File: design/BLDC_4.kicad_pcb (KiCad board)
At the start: 4 copper layers, 38.5 x 65 mm, 126 parts, among them K1 SERVO, P1 HALL/Encoder, P101 CANBUS, P2 SWD, P3 PWR_COMM, P4 IN+, P5 IN-, P6 MOTOR1, P7 MOTOR2, P9 MOTOR3, Q1 IRFS7530, Q2 IRFS7530, Q3 IRFS7530, Q4 IRFS7530, Q5 IRFS7530, Q6 IRFS7530, U1 STM32F40X_LQFP64, U2 TC2117, U3 DRV8302, U401 SN65HVD232, X1 MINI-USB-SHIELD-32005-201, X2 8MHz 10ppm

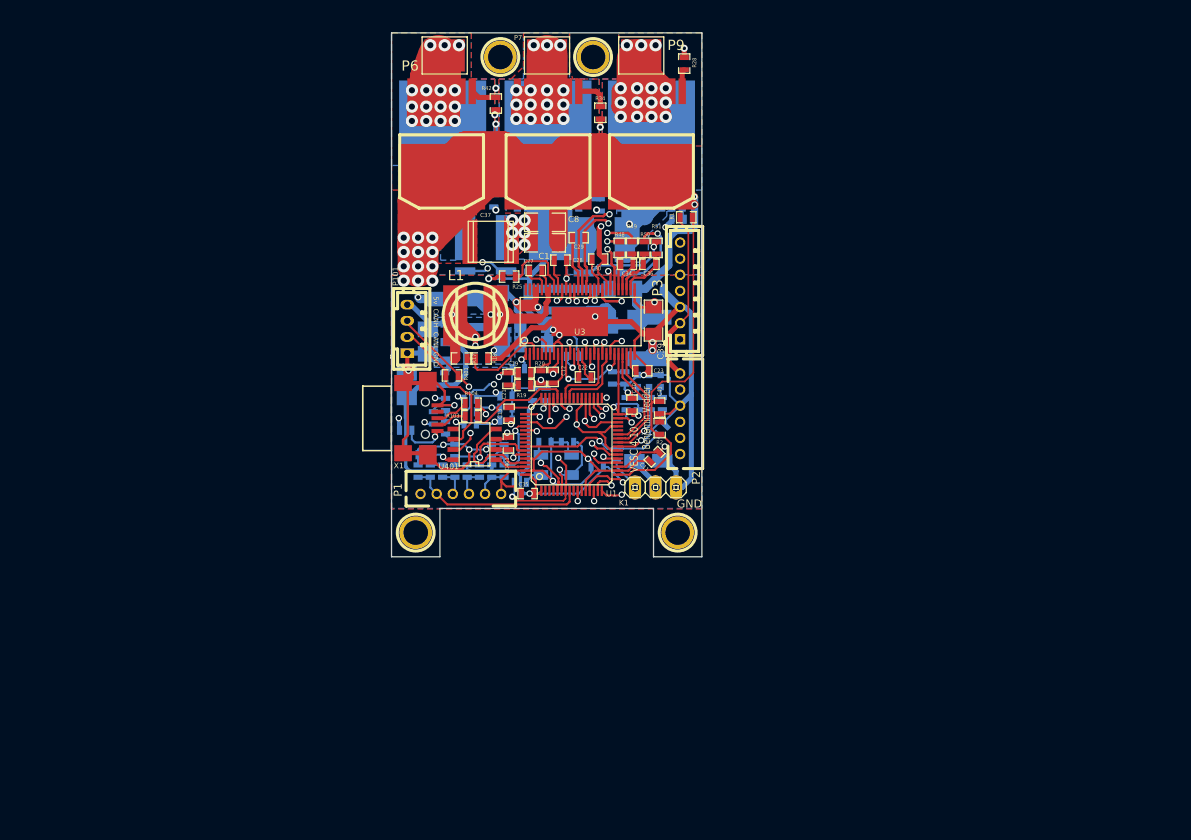
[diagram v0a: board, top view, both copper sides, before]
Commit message: schema mods done
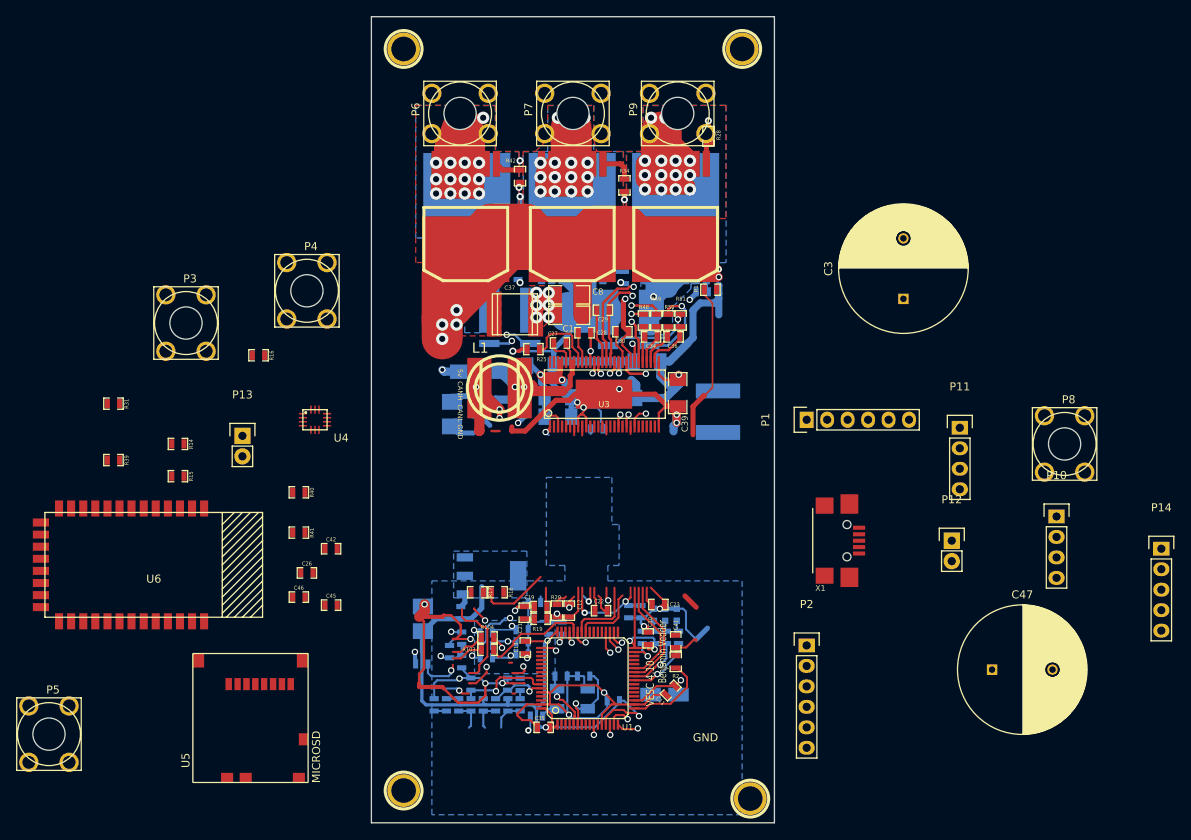
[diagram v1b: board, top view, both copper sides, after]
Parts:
- removed C401: 2.2u, CRF1:SMD-0603_c
- removed K1: SERVO, CRF1:pinhead-1X03
- removed P101: CANBUS, JST conn:b4b-ph-kl
- removed R401: NI, CRF1:SMD-0603_r
- removed R402: 10k, CRF1:SMD-0603_r
- removed R5: 2k2, CRF1:SMD-0603_r
- removed U401: SN65HVD232, CRF1:SOIC-8-W
- added C26: 2.2u, CRF1:SMD-0603_c, F.Cu at (68.0, 147.0)
- added C42: 100nF, CRF1:SMD-0603_c, F.Cu at (71.0, 144.0)
- added C45: 100nF, CRF1:SMD-0603_c, F.Cu at (71.0, 151.0)
- added C46: 2.2u, CRF1:SMD-0603_c, F.Cu at (67.0, 150.0)
- added C47: 680µF, Capacitors_ThroughHole:C_Radial_D16_L25_P7.5, F.Cu at (153.0, 159.0)
- added P10: EXT_I2C, Pin_Headers:Pin_Header_Straight_1x04, F.Cu at (161.0, 140.0)
- added P11: OLED, Pin_Headers:Pin_Header_Straight_1x04, F.Cu at (149.0, 129.0)
- added P12: BRAKE, Pin_Headers:Pin_Header_Straight_1x02, F.Cu at (148.0, 143.0)
- added P13: BUTTONS, Pin_Headers:Pin_Header_Straight_1x02, F.Cu at (60.0, 130.0)
- added P14: EXTENSION, Pin_Headers:Pin_Header_Straight_1x05, F.Cu at (174.0, 144.0)
- added P8: GND_OUT, KEYS7775:KEYS7775, F.Cu at (162.0, 131.0)
- added R14: 2k, CRF1:SMD-0603_r, F.Cu at (52.0, 131.0)
- added R15: 2k, CRF1:SMD-0603_r, F.Cu at (52.0, 135.0)
- added R16: 2k, CRF1:SMD-0603_r, F.Cu at (62.0, 120.0)
- added R31: 2k, CRF1:SMD-0603_r, F.Cu at (44.0, 126.0)
- added R39: 4k7, CRF1:SMD-0603_r, F.Cu at (44.0, 133.0)
- added R40: 4k7, CRF1:SMD-0603_r, F.Cu at (67.0, 137.0)
- added R41: 4k7, CRF1:SMD-0603_r, F.Cu at (67.0, 142.0)
- added U4: LSM6DS3, LSM6DS3:LSM6DS3, F.Cu at (69.0, 128.0)
- added U5: MICROSD, microsd:MOLEX_502570-0893, F.Cu at (61.0, 165.0)
- added U6: BLUETOOTH_SPP-CA, bluetooth_spp-ca:bluetooth_spp-ca, F.Cu at (49.0, 146.0)
- C3: value 100n -> 680µF; footprint CRF1:SMD-0603_c -> Capacitors_ThroughHole:C_Radial_D16_L25_P7.5; moved to F.Cu
- P1, P2: footprint CRF1:MICRO_JST_6 -> Pin_Headers:Pin_Header_Straight_1x06
- P3: value PWR_COMM -> 5V_OUT; footprint CRF1:b7b-ph-kl -> KEYS7775:KEYS7775
- P4, P5: footprint CRF1:1PAD_4x5mm -> KEYS7775:KEYS7775; moved to F.Cu
- P6, P7, P9: footprint CRF1:1PAD_4x5mm -> KEYS7775:KEYS7775
- moved P5 86.9 mm to (36.0, 167.0)
- moved P3 61.4 mm to (53.0, 116.0), turned to 0 degrees
- moved X1 54.5 mm to (135.0, 143.0)
- moved 1PIN 53.0 mm to (123.0, 175.0)
- moved 1PIN 46.7 mm to (80.0, 174.0)
- moved P1 43.9 mm to (130.0, 128.0), turned to 90 degrees
- moved C3 34.1 mm to (142.0, 113.0), turned to 90 degrees
- moved P2 32.8 mm to (130.0, 156.0), turned to 0 degrees
- moved C14 29.1 mm to (98.0, 153.8)
- moved C17 29.1 mm to (99.7, 153.8)
- moved C25 29.1 mm to (82.4, 152.7)
- moved R103 29.1 mm to (90.4, 156.6)
- moved R19 29.1 mm to (97.0, 152.7)
- moved R27 29.1 mm to (94.7, 155.6)
- moved R33 29.1 mm to (94.7, 154.1)
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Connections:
- C3 pad 1: GND -> V_SUPPLY
- C3 pad 2: /MCU/SERVO -> GND
- P2 pad 6: Net-(P2-Pad6) -> TRACESWO
- U1 pad 2: Net-(U1-Pad2) -> /Filters/HALL3_OUT
- U1 pad 20: /MCU/TX_SDA_NSS -> SPI1_SENSOR_CS
- U1 pad 21: /MCU/SCK_ADC_EXT -> SPI1_SCK
- U1 pad 22: /MCU/MISO_ADC_EXT2 -> SPI1_MISO
- U1 pad 23: /MCU/RX_SCL_MOSI -> SPI1_MOSI
- U1 pad 29: /MCU/RX_SCL_MOSI -> /MCU/OLED_I2C_SCL
- U1 pad 30: /MCU/TX_SDA_NSS -> /MCU/OLED_I2C_SDA
- U1 pad 33: /MCU/DC_CAL -> /MCU/BRAKE_IN
- U1 pad 37: /MCU/TX_SDA_NSS -> BLUETOOTH_RX
- U1 pad 38: /MCU/RX_SCL_MOSI -> BLUETOOTH_TX
- U1 pad 50: Net-(U1-Pad50) -> /MCU/DC_CAL
- U1 pad 51: /MCU/EN_GATE -> SPI3_SCK
- U1 pad 52: /Filters/HALL3_OUT -> SPI3_MISO
- U1 pad 53: /MCU/FAULT -> SPI3_MOSI
- U1 pad 54: Net-(U1-Pad54) -> SPI3_SDCARD_CS
- U1 pad 55: Net-(U1-Pad55) -> TRACESWO
- U1 pad 56: Net-(U1-Pad56) -> /MCU/EN_GATE
- U1 pad 57: /MCU/SERVO -> SENSOR_IRQ
- U1 pad 61: /CAN bus transceiver/CAN_RX -> /MCU/FAULT
- U1 pad 62: /CAN bus transceiver/CAN_TX -> Net-(U1-Pad62)
- U1 pad 9: Net-(U1-Pad9) -> /MCU/BUTTONS_IN
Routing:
- net +5V: track 115.3 -> 38.5 mm
- net GND: track 397.8 -> 346.5 mm
- net (no net): track 0.00 -> 50.3 mm, vias 0 -> 5
- net /Mosfet driver/M_H1: track 49.8 -> 0.00 mm, vias 2 -> 0
- net /MCU/TX_SDA_NSS: track 47.1 -> 0.00 mm, vias 2 -> 0
- net /MCU/RX_SCL_MOSI: track 41.6 -> 0.00 mm, vias 1 -> 0
- net /MCU/MISO_ADC_EXT2: track 36.0 -> 0.00 mm, vias 1 -> 0
- net /MCU/ADC_TEMP: track 44.0 -> 11.8 mm
- net NRST: track 32.6 -> 1.95 mm, vias 2 -> 1
- net /MCU/SCK_ADC_EXT: track 26.4 -> 0.00 mm, vias 1 -> 0
- net V_SUPPLY: track 239.3 -> 214.3 mm, vias 18 -> 10
- net SWDIO: track 23.2 -> 0.00 mm, vias 1 -> 0
- net /CAN bus transceiver/CANH: track 21.2 -> 0.00 mm, vias 2 -> 0
- net /Filters/TEMP_IN: track 22.4 -> 1.52 mm
- net /MCU/EN_GATE: track 19.6 -> 0.00 mm, vias 2 -> 0
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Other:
- board size 38.5 x 65 mm -> 50 x 100 mm
- board text removed: "3.3V"
- board text removed: "3.3v"
- board text removed: "ADC"
- board text removed: "ADC2"
- board text removed: "CLK"
- board text removed: "DIO"
- board text removed: "H1"
- board text removed: "H2"
- board text removed: "H3"
- board text removed: "MISO"
- board text removed: "MOSI"
- board text removed: "NSS"
- board text removed: "RST"
- board text removed: "RX"
- board text removed: "SCK"
- board text removed: "SCL"
- board text removed: "SDA"
- board text removed: "TEMP"
- board text removed: "TX"
